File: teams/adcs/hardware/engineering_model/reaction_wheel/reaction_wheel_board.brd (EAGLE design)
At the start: 94 x 94 mm, 80 parts

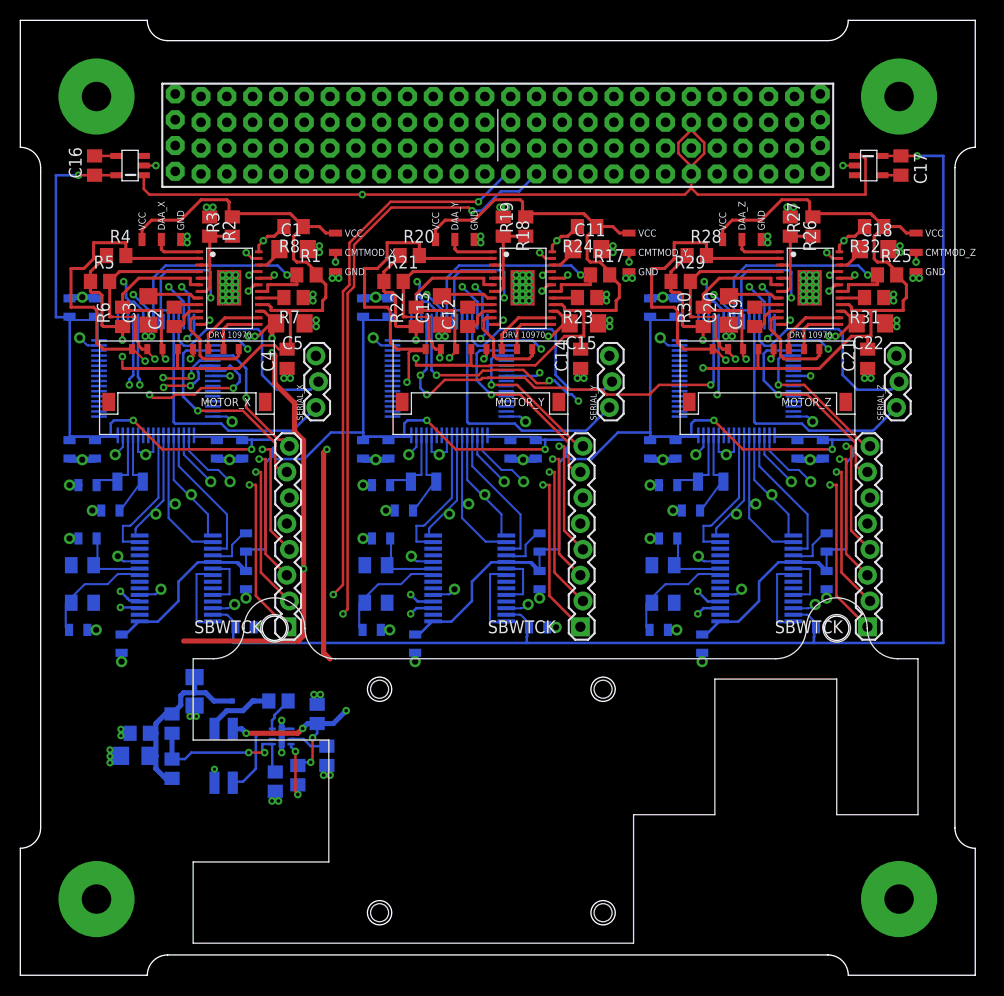
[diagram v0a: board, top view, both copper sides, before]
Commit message: ADCS/RW: Rearrange circuit to make room for bracket
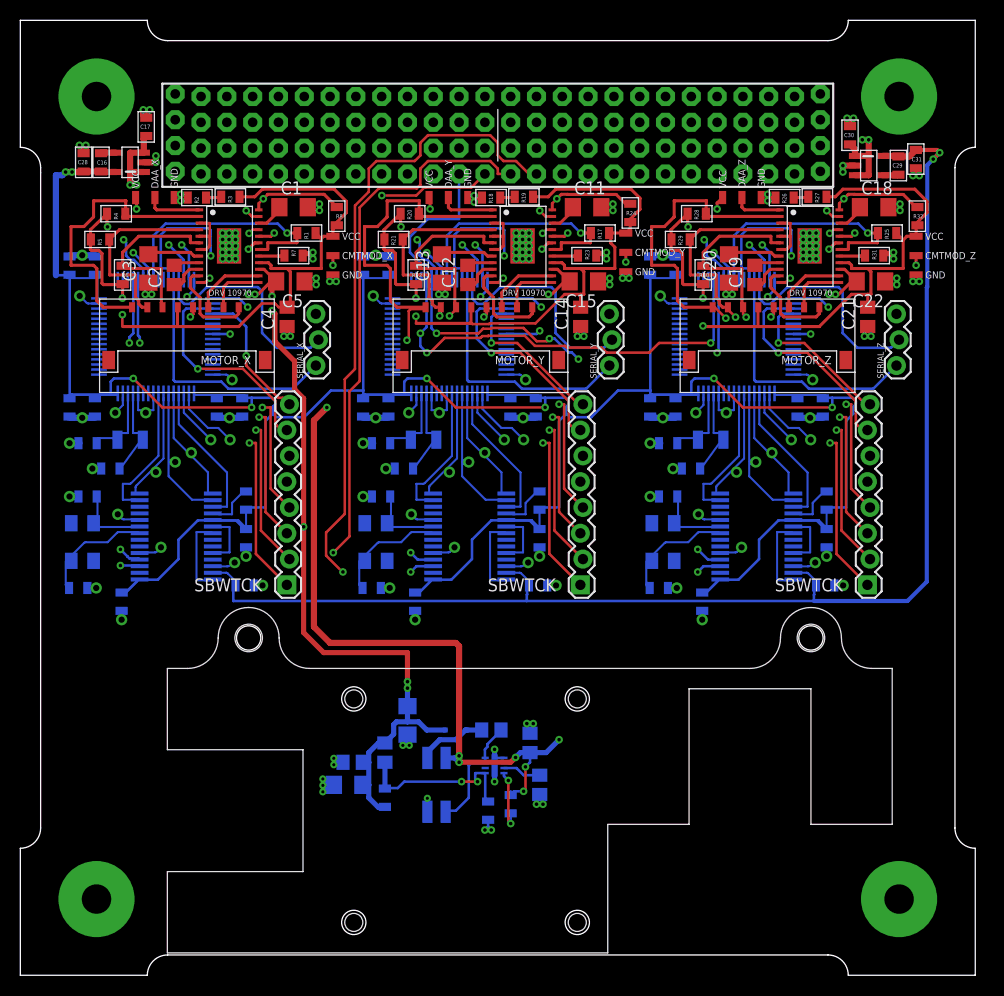
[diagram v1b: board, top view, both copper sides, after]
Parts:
- removed LDO_3V3: LINEAR_LDO_LT1761-X, DubSat1 Components:SOT-23-5
- added C28, C30: 1 μF, DubSat1 Components:0805
- added C29: 0.01 μF, DubSat1 Components:0805
- added C31: 1μF, DubSat1 Components:0805
- added U2: TPS732XX, DubSat1 Components:SOT-23-5
- C16: device rcl:C0805 -> DubSat1 Components:0805
- C17: value 0.01 μF -> 1 μF; device rcl:C0805 -> DubSat1 Components:0805
- R1, R12, R13, R14, R17, R18, R19, R2, R20, R21, R22, R23, R24, R25, R26, R27, R28, R29, R3, R30, R31, R32, R4, R5, R6, R7, R8: device rcl:R0805 -> DubSat1 Components:0805
- U3: value LINEAR_LDO_LT1761-X -> TPS732XX
- moved C17 74.4 mm to (11.1, 82.2)
- moved C23 21.1 mm to (48.9, 21.6)
- moved C25 21.1 mm to (45.1, 22.9)
- moved C27 21.1 mm to (34.6, 20.6)
- moved C6 21.1 mm to (31.4, 19.7)
- moved D2 21.1 mm to (41.6, 22.9)
- moved R12 21.1 mm to (47.0, 15.6)
- moved R13 21.1 mm to (34.6, 16.2)
- moved U$5 21.1 mm to (45.4, 19.4)
- moved C24 21.1 mm to (49.8, 17.5)
- moved C26 21.1 mm to (36.8, 23.8)
- moved C7 21.1 mm to (31.0, 17.5)
- moved L2 21.1 mm to (39.7, 17.5)
- moved R14 21.1 mm to (44.8, 14.9)
- moved R24 4.46 mm to (58.8, 73.8), turned to 90 degrees
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- renumbered LDO_5V to U3
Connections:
- removed net N$13: C17.2, U3.P$4
- removed net N$14: C16.2, LDO_3V3.P$4
- new net LDO_3V3_BYP2: C16.2, U2.P$4
- new net LDO_5V_BYP: C29.2, U3.P$4
- net +3V3: now also C28.2, U2.P$5; no longer LDO_3V3.P$5
- net +5V: now also C29.1, C31.2; no longer C17.1
- net GND: now also C17.1, C28.1, C30.1, C31.1, U2.P$2; no longer LDO_3V3.P$2
- net VBAT: now also C17.2, C30.2, U2.P$1, U2.P$3, U3.P$3; no longer LDO_3V3.P$1
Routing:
- net VBAT: track 157.0 -> 182.4 mm, vias 7 -> 11
- net HP_U_X: track 48.7 -> 29.9 mm, vias 3 -> 0
- net HP_V_X: track 30.4 -> 19.3 mm, vias 3 -> 0
- net HP_W_X: track 27.5 -> 17.9 mm, vias 3 -> 0
- net VM: track 173.5 -> 182.2 mm, vias 8 -> 10
- net VINT_X: track 79.2 -> 71.1 mm, vias 2 -> 4
- net VINT_Z: track 79.4 -> 71.5 mm, vias 2 -> 4
- net GND: track 118.2 -> 125.9 mm, vias 117 -> 121
- net VINT_Y: track 78.8 -> 71.4 mm, vias 2 -> 4
- net SYNC1: track 115.0 -> 109.0 mm
- net FG_X: track 24.3 -> 29.6 mm
- net FG_Z: track 24.3 -> 29.6 mm
- net +3V3: track 243.7 -> 238.4 mm, vias 7 -> 8
- net FG_Y: track 24.3 -> 29.5 mm
- net CANL: track 121.8 -> 127.0 mm, vias 5 -> 4
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- added copper zone on layer 3, net VBAT

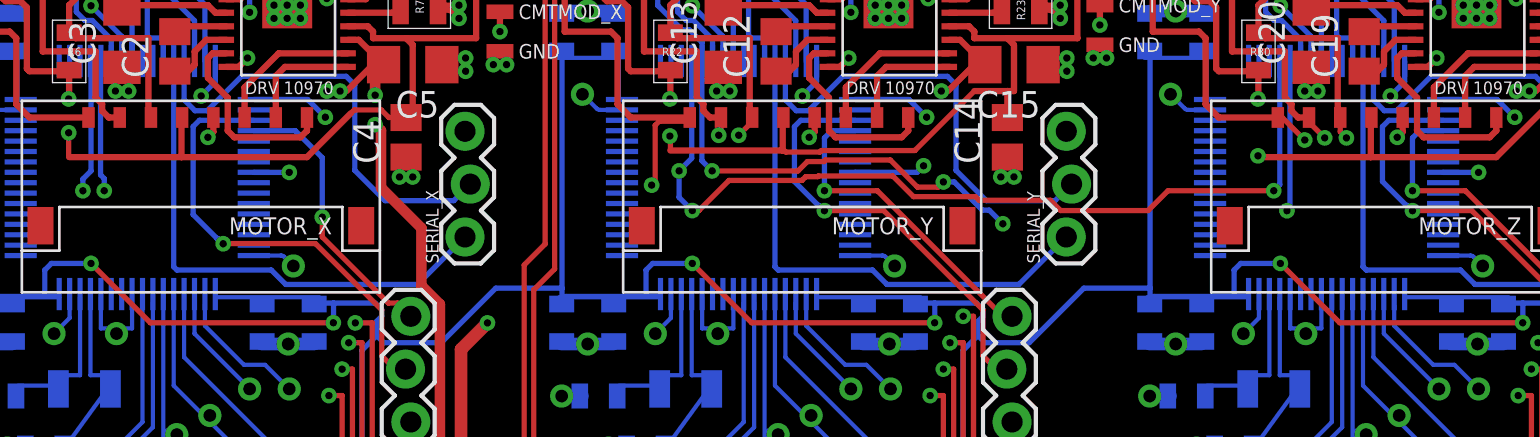
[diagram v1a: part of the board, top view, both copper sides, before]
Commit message: ADCS/RW: Add LEDs to RW board
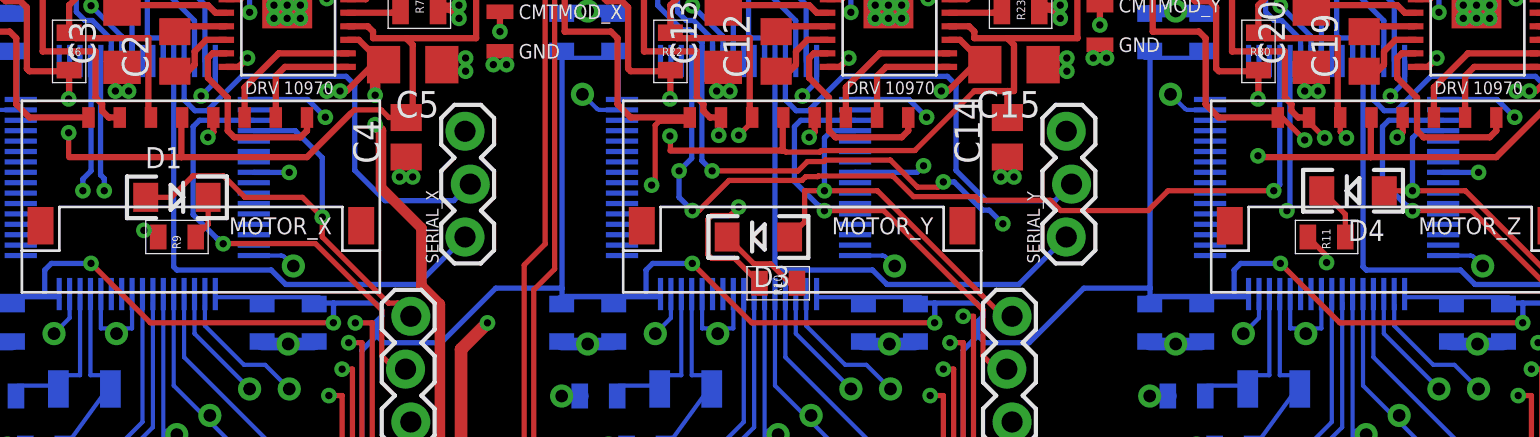
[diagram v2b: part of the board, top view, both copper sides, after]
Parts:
- added D1, D3, D4: (no value), DubSat1 Components:LED-1206
- added R10, R11, R9: (no value), DubSat1 Components:0805
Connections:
- new net N$2: D4.C, R11.2
- new net N$3: D3.C, R10.2
- new net N$4: D1.C, R9.2
- net GND: now also R10.1, R11.1, R9.1
- net GPIO_DEBUG_3.5_X: now also D1.A
- net GPIO_DEBUG_3.5_Y: now also D3.A
- net GPIO_DEBUG_3.5_Z: now also D4.A
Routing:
- net GPIO_DEBUG_3.5_X: track 13.9 -> 23.6 mm
- net GND: track 125.9 -> 134.8 mm, vias 121 -> 124
- net N$3: track 0.00 -> 4.27 mm
- net GPIO_DEBUG_3.5_Y: track 15.7 -> 19.1 mm
- net N$2: track 0.00 -> 2.69 mm
- net N$4: track 0.00 -> 2.15 mm
- net GPIO_DEBUG_3.5_Z: track 15.7 -> 17.0 mm
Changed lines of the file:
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@@
 <element name="C30" library="DubSat1 Components" package="0805" value="1 μF" x="80.391" y="81.407" rot="R270"/>
 <element name="C31" library="DubSat1 Components" package="0805" value="1μF" x="86.868" y="79.0575" rot="R90"/>
+<element name="D1" library="DubSat1 Components" package="LED-1206" value="" x="13.97" y="60.6425"/>
+<element name="D3" library="DubSat1 Components" package="LED-1206" value="" x="41.91" y="58.7375" rot="R180"/>
+<element name="D4" library="DubSat1 Components" package="LED-1206" value="" x="70.485" y="60.96" rot="R180"/>
+<element name="R9" library="DubSat1 Components" package="0805" value="" x="13.97" y="58.7375"/>
+<element name="R10" library="DubSat1 Components" package="0805" value="" x="42.8625" y="56.515"/>
+<element name="R11" library="DubSat1 Components" package="0805" value="" x="69.215" y="58.7375"/>
 </elements>
 <signals>
@@
 <wire x1="24.13" y1="55.5625" x2="24.5745" y2="55.5625" width="0.254" layer="1"/>
 <wire x1="24.5745" y1="55.5625" x2="25.2095" y2="54.9275" width="0.254" layer="1"/>
+<contactref element="D1" pad="A"/>
+<wire x1="14.733225" y1="61.6727" x2="16.206775" y2="61.6727" width="0.254" layer="1"/>
+<wire x1="20.0025" y1="60.6425" x2="20.955" y2="59.69" width="0.254" layer="1"/>
+<wire x1="12.47" y1="60.6425" x2="13.703025" y2="60.6425" width="0.254" layer="1"/>
+<wire x1="17.236975" y1="60.6425" x2="20.0025" y2="60.6425" width="0.254" layer="1"/>
+<wire x1="13.703025" y1="60.6425" x2="14.733225" y2="61.6727" width="0.254" layer="1"/>
+<wire x1="16.206775" y1="61.6727" x2="17.236975" y2="60.6425" width="0.254" layer="1"/>
 </signal>
 <signal name="GND">
@@
 <wire x1="73.05045" y1="75.27511875" x2="72.73238125" y2="74.95705" width="0.3048" layer="1"/>
 <wire x1="72.73238125" y1="74.95705" x2="72.0725" y2="74.95705" width="0.3048" layer="1"/>
+<contactref element="R10" pad="1"/>
+<contactref element="R11" pad="1"/>
+<contactref element="R9" pad="1"/>
+<via x="12.3825" y="59.055" extent="1-16" drill="0.35" shape="square"/>
+<wire x1="12.3825" y1="59.055" x2="12.7525" y2="59.055" width="0.254" layer="1"/>
+<wire x1="12.7525" y1="59.055" x2="13.07" y2="58.7375" width="0.254" layer="1"/>
+<wire x1="39.673225" y1="57.7073" x2="39.4798" y2="57.900725" width="0.254" layer="1"/>
+<wire x1="39.4798" y1="57.900725" x2="39.4798" y2="59.574275" width="0.254" layer="1"/>
+<wire x1="39.4798" y1="59.574275" x2="39.673225" y2="59.7677" width="0.254" layer="1"/>
+<wire x1="39.673225" y1="59.7677" x2="40.54964375" y2="59.7677" width="0.254" layer="1"/>
+<wire x1="40.54964375" y1="59.7677" x2="40.9575" y2="60.17555625" width="0.254" layer="1"/>
+<wire x1="40.7702" y1="57.7073" x2="39.673225" y2="57.7073" width="0.254" layer="1"/>
+<wire x1="41.9625" y1="56.515" x2="40.7702" y2="57.7073" width="0.254" layer="1"/>
+<via x="40.9575" y="60.17555625" extent="1-16" drill="0.35" shape="square"/>
+<wire x1="68.315" y1="58.7375" x2="69.215" y2="57.8375" width="0.254" layer="1"/>
+<wire x1="69.215" y1="57.8375" x2="69.215" y2="57.50805625" width="0.254" layer="1"/>
+<via x="69.215" y="57.50805625" extent="1-16" drill="0.35" shape="square"/>
 </signal>
 <signal name="CANH">
@@
 <wire x1="53.6575" y1="54.9275" x2="54.102" y2="54.9275" width="0.254" layer="1"/>
 <wire x1="47.625" y1="60.96" x2="53.6575" y2="54.9275" width="0.254" layer="1"/>
+<contactref element="D3" pad="A"/>
+<wire x1="43.41" y1="58.7375" x2="44.1325" y2="59.46" width="0.254" layer="1"/>
+<wire x1="44.1325" y1="59.46" x2="44.1325" y2="60.96" width="0.254" layer="1"/>
+<wire x1="44.1325" y1="60.96" x2="45.085" y2="60.96" width="0.254" layer="1"/>
 </signal>
 <signal name="PWM_Y">
@@
 <wire x1="81.915" y1="54.9275" x2="82.3595" y2="54.9275" width="0.254" layer="1"/>
 <wire x1="75.8825" y1="60.96" x2="81.915" y2="54.9275" width="0.254" layer="1"/>
+<contactref element="D4" pad="A"/>
+<wire x1="71.985" y1="60.96" x2="73.3425" y2="60.96" width="0.254" layer="1"/>
 </signal>
 <signal name="PWM_Z">
@@
 <wire x1="85.1035" y1="77.4725" x2="85.1535" y2="77.5225" width="0.6096" layer="1"/>
 </signal>
+<signal name="N$2">
+<contactref element="R11" pad="2"/>
+<contactref element="D4" pad="C"/>
+<wire x1="68.985" y1="60.96" x2="70.115" y2="59.83" width="0.254" layer="1"/>
+<wire x1="70.115" y1="59.83" x2="70.115" y2="58.7375" width="0.254" layer="1"/>
+</signal>
+<signal name="N$3">
+<contactref element="R10" pad="2"/>
+<contactref element="D3" pad="C"/>
+<wire x1="42.499275" y1="57.4452" x2="41.7023" y2="57.4452" width="0.254" layer="1"/>
+<wire x1="41.7023" y1="57.4452" x2="40.41" y2="58.7375" width="0.254" layer="1"/>
+<wire x1="43.7625" y1="56.515" x2="43.429475" y2="56.515" width="0.254" layer="1"/>
+<wire x1="43.429475" y1="56.515" x2="42.499275" y2="57.4452" width="0.254" layer="1"/>
+</signal>
+<signal name="N$4">
+<contactref element="R9" pad="2"/>
+<contactref element="D1" pad="C"/>
+<wire x1="14.87" y1="58.7375" x2="15.47" y2="59.3375" width="0.254" layer="1"/>
+<wire x1="15.47" y1="59.3375" x2="15.47" y2="60.6425" width="0.254" layer="1"/>
+</signal>
 </signals>

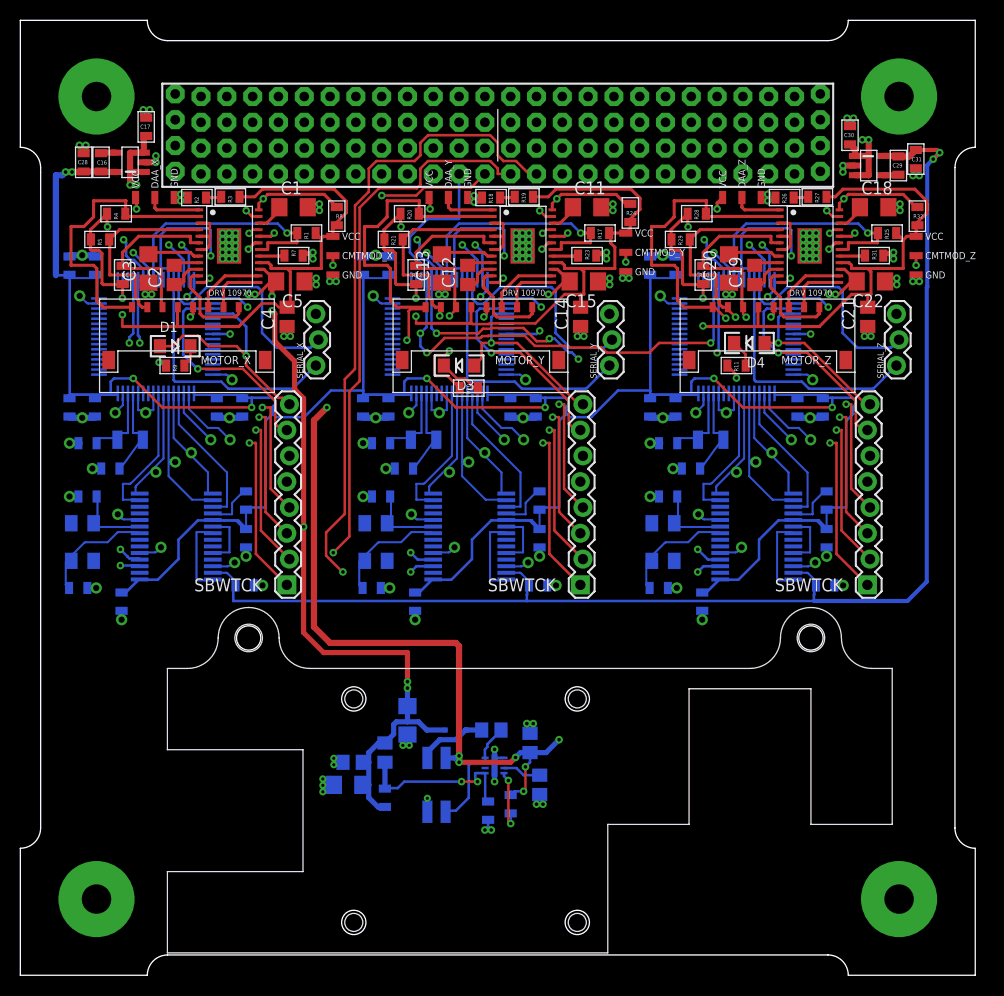
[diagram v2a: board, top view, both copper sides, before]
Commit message: ADCS/RW: Add debugging outputs for FG and PWM
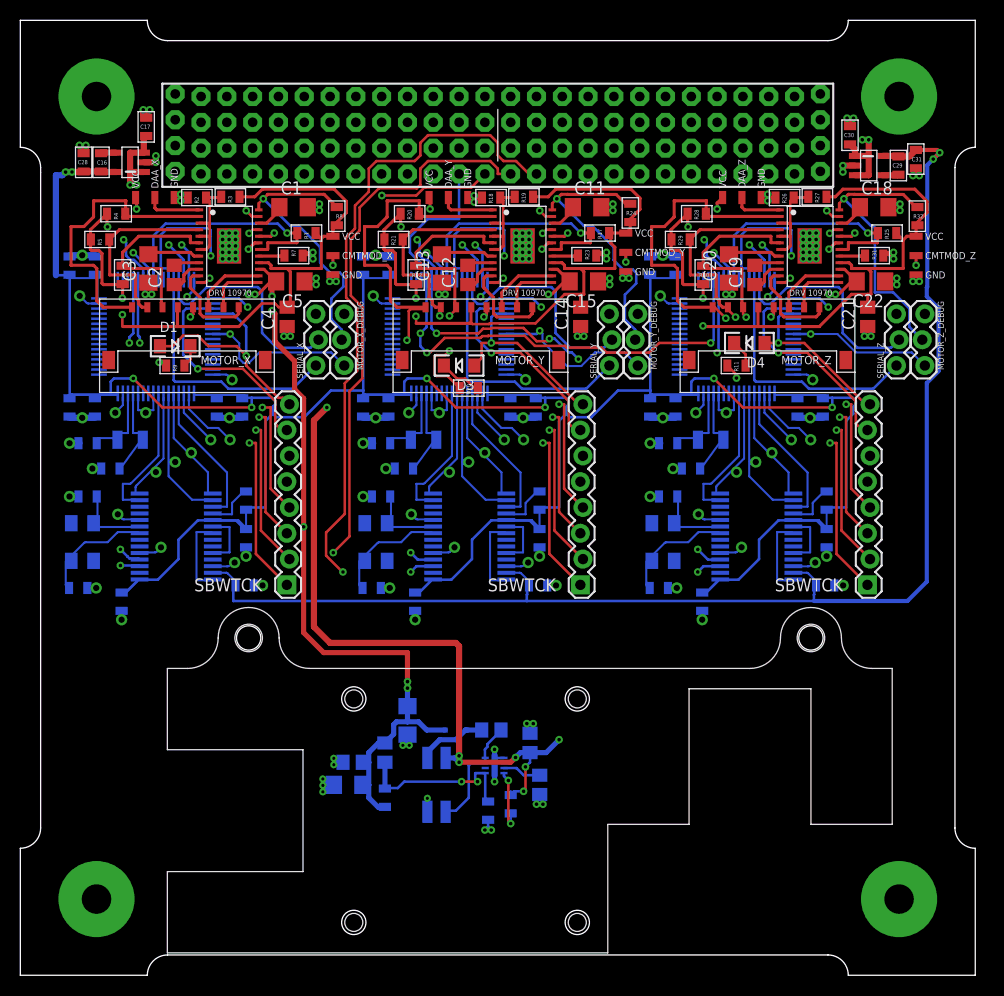
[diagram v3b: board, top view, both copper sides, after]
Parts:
- added MOTOR_X_DEBUG, MOTOR_Y_DEBUG, MOTOR_Z_DEBUG: (no value), SparkFun-Connectors:1X03_LOCK
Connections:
- net FG_X: now also MOTOR_X_DEBUG.2
- net FG_Y: now also MOTOR_Y_DEBUG.2
- net FG_Z: now also MOTOR_Z_DEBUG.2
- net GND: now also MOTOR_X_DEBUG.1, MOTOR_Y_DEBUG.1, MOTOR_Z_DEBUG.1
- net PWM_X: now also MOTOR_X_DEBUG.3
- net PWM_Y: now also MOTOR_Y_DEBUG.3
- net PWM_Z: now also MOTOR_Z_DEBUG.3
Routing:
- net FG_X: track 29.6 -> 48.7 mm
- net FG_Y: track 29.5 -> 48.5 mm
- net FG_Z: track 29.6 -> 47.8 mm
- net PWM_X: track 12.6 -> 26.9 mm
- net PWM_Y: track 13.4 -> 26.0 mm
- net PWM_Z: track 12.6 -> 25.2 mm
- net HN_X: track 6.96 -> 10.00 mm
- net HN_Z: track 6.90 -> 9.92 mm
- net HN_Y: track 6.90 -> 9.59 mm
- net +5V: track 123.4 -> 124.3 mm
- net CANH: track 119.6 -> 120.6 mm
- net CANL: track 127.0 -> 127.9 mm
- net VBAT: track 182.4 -> 182.9 mm
